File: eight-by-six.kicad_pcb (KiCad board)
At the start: 2 copper layers, 171.4 x 133.4 mm, 6 parts

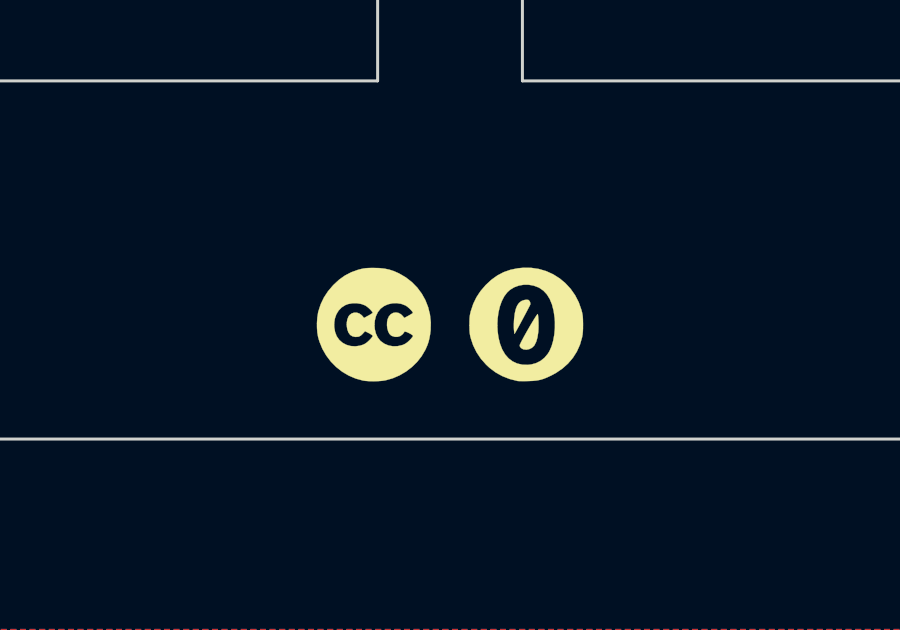
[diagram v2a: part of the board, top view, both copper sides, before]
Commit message: pcb -- adjust the position of 'CC' and '0' logos
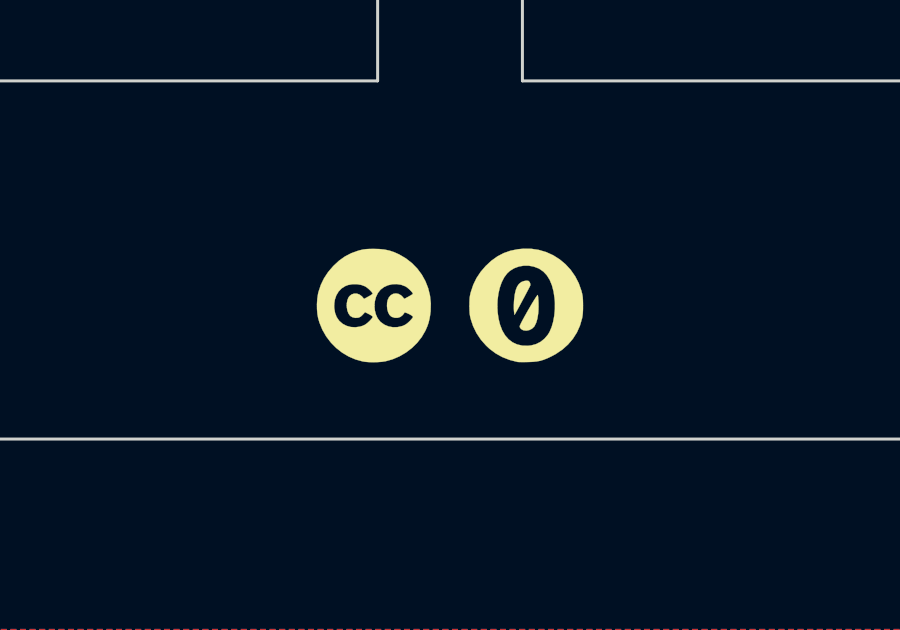
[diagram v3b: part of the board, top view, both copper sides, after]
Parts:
- moved G*** 0.63 mm to (102.2, 243.2)
- moved G*** 0.63 mm to (107.3, 243.2)
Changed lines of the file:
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@@
   )
   (footprint "cliparts:logo--cc--cc" locked (layer "F.Cu")
-    (at 102.235 243.84)
+    (at 102.235 243.205)
     (attr through_hole)
     (fp_text reference "G***" (at 0 0) (layer "F.SilkS") hide
@@
   )
   (footprint "cliparts:logo--cc--zero" locked (layer "F.Cu")
-    (at 107.315 243.84)
+    (at 107.315 243.205)
     (attr through_hole)
     (fp_text reference "G***" (at 0 0) (layer "F.SilkS") hide
